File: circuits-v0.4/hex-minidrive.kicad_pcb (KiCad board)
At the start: 4 copper layers, 18 x 48 mm, 81 parts, among them X1 16MHz

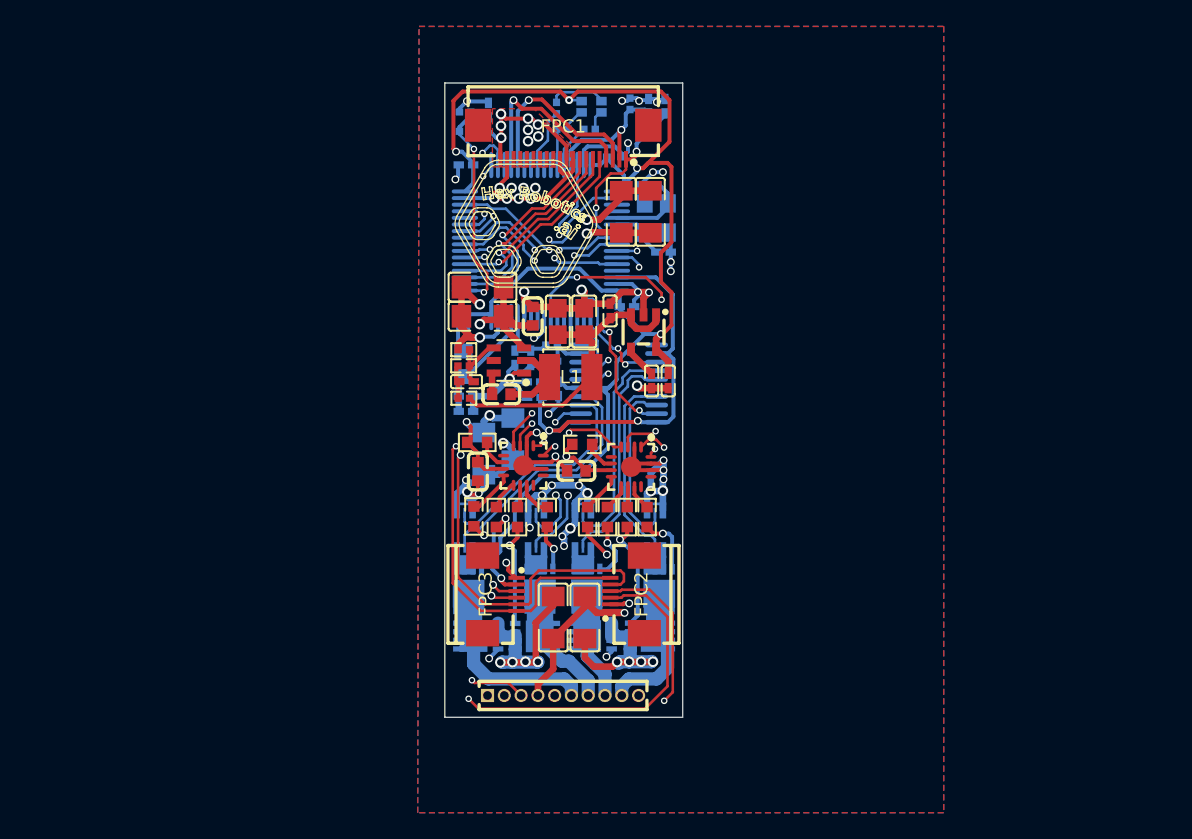
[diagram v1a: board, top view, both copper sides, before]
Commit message: Make schematic for v0.4 driver circuit.
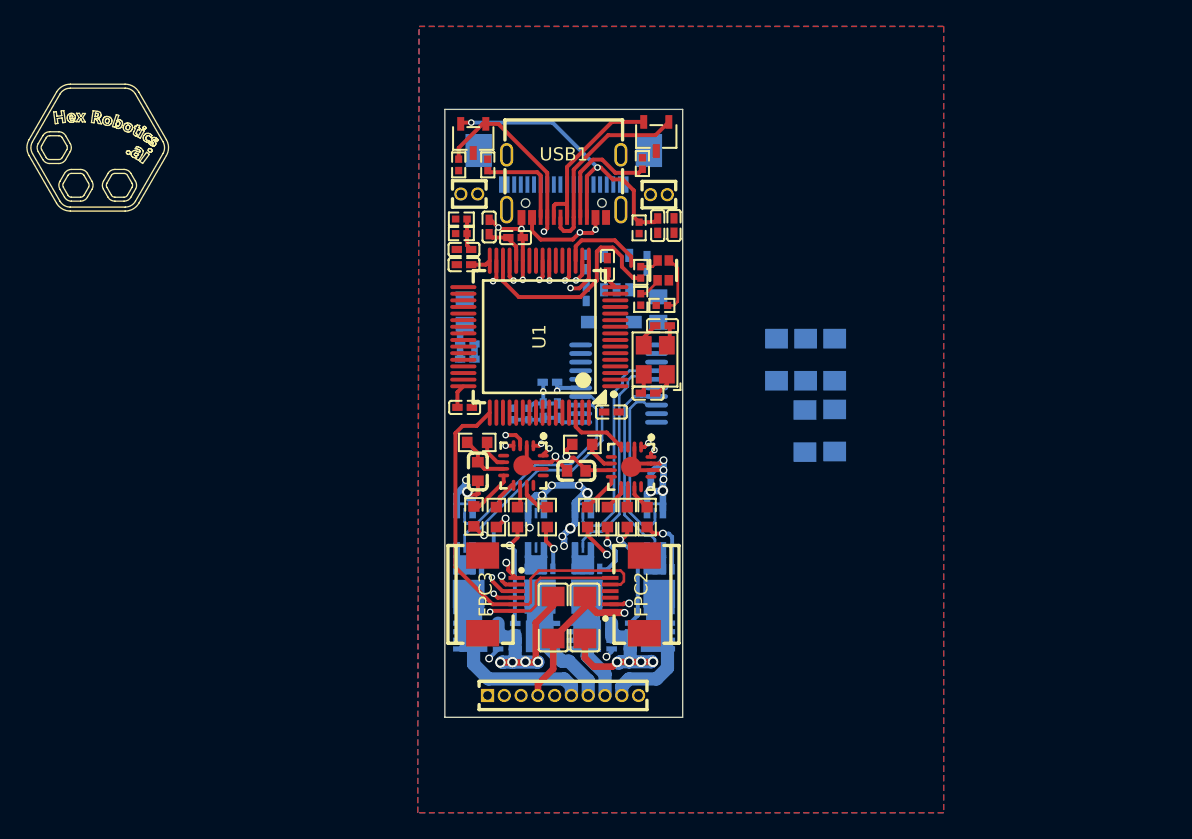
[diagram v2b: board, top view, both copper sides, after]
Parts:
- removed C41: 10uF, Library:C1206
- removed C42, C43: 100nF, Library:C0603
- removed C44, C45: 22uF, Library:C0805
- removed C46: 100pF, Library:C0402
- removed L1: 15uH, Library:IND-SMD_L4.0-W4.0
- removed R41: 49.9Ω, Library:R0402
- removed R42: 100kΩ, Library:R0402
- removed R43: 13.3kΩ, Library:R0402
- removed U4: ~, Library:SOT-23-6_L2.9-W1.6-P0.95-LS2.8-BL
- added D1: ~, Library:SOD-123_L2.7-W1.6-LS3.7-RD-1, B.Cu at (31.6, 38.1)
- added D2: ~, Library:SOT-23-3_L3.0-W1.7-P0.95-LS2.9-BR, F.Cu at (35.0, 24.1)
- added D3: ~, Library:SOT-23-3_L3.0-W1.7-P0.95-LS2.9-BR, F.Cu at (21.1, 24.2)
- added H2: 2P-1.27mm-header, Library:HDR-TH_2P-P1.27-V-M-2, F.Cu at (35.2, 28.4)
- added H3: 2P-1.27mm-header, Library:HDR-TH_2P-P1.27-V-M-2, F.Cu at (20.9, 28.4)
- added L3: 300mΩ, Library:L0805, B.Cu at (35.1, 37.1)
- added R14: 10kΩ, Library:R0402, F.Cu at (20.1, 26.2)
- added R5: 5.1kΩ, Library:R0402, F.Cu at (22.2, 26.2)
- added R6: 5.1kΩ, Library:R0402, F.Cu at (34.0, 26.1)
- added USB1: ~, Library:USB-C-SMD_TYPE-C16PIN, F.Cu at (28.0, 27.8)
- C103, C104, C105, C106, C109, C110, C111, C112, C113, C114, C115, LED1, R11, R15, R16, R17, R18, R19, U1, X1: moved to F.Cu
- C2, C3, C31, C32, C33, C5, FPC1, U3: moved to B.Cu
- moved C4 24.4 mm to (46.2, 46.3)
- moved C6 24.4 mm to (48.5, 46.3)
- moved C5 22.9 mm to (44.1, 40.9), turned to 90 degrees
- moved C111 19.3 mm to (31.6, 44.9)
- moved C2 17.9 mm to (48.5, 40.9), turned to 90 degrees
- moved C3 17.9 mm to (46.3, 40.9), turned to 90 degrees
- moved R16 16.9 mm to (35.4, 36.8), turned to 180 degrees
- moved C103 15.8 mm to (34.4, 43.5)
- moved C112 14.5 mm to (20.5, 44.5)
- moved R17 14.2 mm to (33.8, 36.4), turned to 90 degrees
- moved LED1 13.5 mm to (35.5, 34.2), turned to -90 degrees
- moved C109 13.1 mm to (31.3, 33.8), turned to -90 degrees
- moved R15 11.5 mm to (33.8, 34.3), turned to -90 degrees
- moved X1 10.7 mm to (34.9, 41.0), turned to 90 degrees
- moved C115 10.7 mm to (20.4, 32.6), turned to 0 degrees
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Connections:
- FPC1 pad 1: NRST -> VCC
- FPC1 pad 12: VCC -> GND
- FPC1 pad 14: VCC -> GND
- FPC1 pad 16: VCC -> GND
- FPC1 pad 18: VCC -> GND
- FPC1 pad 2: BOOT0/STOP -> VCC
- FPC1 pad 20: VCC -> GND
- FPC1 pad 3: USART3_RX -> VCC
- FPC1 pad 4: USART3_TX -> VCC
- FPC1 pad 5: SPI2_MOSI -> VCC
- FPC1 pad 6: SPI2_MISO -> VCC
- FPC1 pad 7: SPI2_SCK -> VCC
- FPC1 pad 8: SPI2_NSS -> VCC
- FPC1 pad 9: GND -> VCC
- R13 pad 2: VREF -> 3V3A
- R15 pad 2: TIM4_CH2/GREEN_LED -> TIM2_CH3/GREEN_LED
- R17 pad 1: TIM4_CH1/RED_LED -> TIM2_CH1/RED_LED
- U1 pad 13: unconnected-(U1-PA1-Pad13) -> TIM2_CH2/BLUE_LED
- U1 pad 19: unconnected-(U1-PA5-Pad19) -> TIM2_CH1/RED_LED
- U1 pad 30: unconnected-(U1-PB10-Pad30) -> TIM2_CH3/GREEN_LED
- U1 pad 34: SPI2_NSS -> unconnected-(U1-PB12-Pad34)
- U1 pad 35: SPI2_SCK -> unconnected-(U1-PB13-Pad35)
- U1 pad 36: SPI2_MISO -> TIM1_CH2N
- U1 pad 37: SPI2_MOSI -> unconnected-(U1-PB15-Pad37)
- U1 pad 45: unconnected-(U1-PA11-Pad45) -> USB_D_N
- U1 pad 46: TIM1_CH2N -> USB_D_P
- U1 pad 52: USART3_TX -> unconnected-(U1-PC10-Pad52)
- U1 pad 53: USART3_RX -> unconnected-(U1-PC11-Pad53)
- U1 pad 56: TIM2_CH2/BLUE_LED -> unconnected-(U1-PB3-Pad56)
- U1 pad 59: TIM4_CH1/RED_LED -> unconnected-(U1-PB6-Pad59)
- U1 pad 60: TIM4_CH2/GREEN_LED -> unconnected-(U1-PB7-Pad60)
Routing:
- net 3V3: track 144.5 -> 27.0 mm, vias 6 -> 3
- net GND: track 165.3 -> 78.0 mm, vias 49 -> 23
- net I2C2_SCL: track 69.6 -> 0.00 mm, vias 2 -> 0
- net I2C2_SDA: track 68.1 -> 0.00 mm, vias 2 -> 0
- net SYS_JTCK-SWCLK: track 51.2 -> 11.2 mm, vias 2 -> 1
- net TIM3_CH2/ENCODER_2: track 39.0 -> 0.00 mm, vias 1 -> 0
- net TIM3_CH1/ENCODER_1: track 37.5 -> 0.00 mm, vias 1 -> 0
- net I2C3_SCL: track 36.6 -> 1.86 mm, vias 2 -> 1
- net VCC: track 73.8 -> 39.3 mm, vias 21 -> 9
- net I2C3_SDA: track 36.3 -> 2.45 mm, vias 2 -> 1
- net TIM3_CH3/ENCODER_3: track 34.1 -> 1.55 mm, vias 2 -> 1
- net ADC1_IN3/HALF_VREF: track 37.2 -> 5.23 mm, vias 2 -> 0
- net TIM1_CH4N: track 25.3 -> 1.51 mm, vias 3 -> 1
- net 5V: track 23.4 -> 0.00 mm
- net TIM1_CH1N: track 23.9 -> 0.60 mm, vias 2 -> 1
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- removed copper zone on F.Cu, net VCC
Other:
- board size 18 x 48 mm -> 18 x 46 mm

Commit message: Almost done re-wiring v0.4
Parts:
- moved C2 24.2 mm to (72.7, 41.0)
- moved C3 24.2 mm to (70.5, 41.0)
- moved C4 24.2 mm to (70.4, 46.4)
- moved C6 24.2 mm to (72.7, 46.3)
- moved C5 24.2 mm to (68.2, 41.0)
- moved L3 10.1 mm to (28.4, 29.7), turned to 0 degrees
- moved C107 7.20 mm to (20.5, 43.2), turned to 0 degrees
- moved C108 6.55 mm to (20.5, 42.0), turned to 0 degrees
- moved R13 6.52 mm to (20.4, 39.8), turned to 180 degrees
- moved R12 6.39 mm to (20.4, 41.0), turned to 0 degrees
- moved C21 5.63 mm to (25.6, 48.1)
- moved C33 5.62 mm to (34.2, 30.2), turned to 180 degrees
- moved D1 5.49 mm to (30.9, 32.6), turned to 90 degrees
- moved C109 4.48 mm to (35.0, 36.2), turned to 0 degrees
- moved U2 4.45 mm to (31.0, 47.0)
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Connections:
- R15 pad 2: TIM2_CH3/GREEN_LED -> TIM2_CH1/GREEN_LED
- R17 pad 1: TIM2_CH1/RED_LED -> TIM2_CH3/RED_LED
- U1 pad 19: TIM2_CH1/RED_LED -> TIM2_CH1/GREEN_LED
- U1 pad 30: TIM2_CH3/GREEN_LED -> TIM2_CH3/RED_LED
- U2 pad 2: ADC1_IN1/M1_CURRENT -> ADC2_IN3/M2_CURRENT
- U2 pad 3: -Probe-1 -> -Probe-2
- U2 pad 4: +Probe-1 -> +Probe-2
- U2 pad 6: +Probe-2 -> +Probe-1
- U2 pad 7: -Probe-2 -> -Probe-1
- U2 pad 8: ADC2_IN3/M2_CURRENT -> ADC1_IN1/M1_CURRENT
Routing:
- net 3V3: track 27.0 -> 123.6 mm, vias 3 -> 7
- net I2C2_SCL: track 0.00 -> 52.5 mm, vias 0 -> 2
- net I2C2_SDA: track 0.00 -> 51.5 mm, vias 0 -> 2
- net ADC1_IN3/HALF_VREF: track 5.23 -> 48.6 mm, vias 0 -> 5
- net TIM3_CH3/ENCODER_3: track 1.55 -> 42.9 mm
- net TIM3_CH2/ENCODER_2: track 0.00 -> 34.1 mm, vias 0 -> 1
- net TIM3_CH1/ENCODER_1: track 0.00 -> 32.6 mm, vias 0 -> 1
- net NRST: track 14.4 -> 44.7 mm, vias 1 -> 4
- net I2C3_SCL: track 1.86 -> 27.5 mm, vias 1 -> 2
- net I2C3_SDA: track 2.45 -> 25.6 mm, vias 1 -> 2
- net BOOT0/STOP: track 23.5 -> 45.1 mm, vias 2 -> 4
- net SYS_JTCK-SWCLK: track 11.2 -> 32.4 mm, vias 1 -> 0
- net ADC2_IN17/M4_CURRENT: track 1.71 -> 22.0 mm
- net TIM1_CH4N: track 1.51 -> 20.3 mm, vias 1 -> 2
- net GND: track 78.0 -> 96.6 mm, vias 23 -> 27
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
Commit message: Tentatively done wiring v0.4.
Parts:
- removed C5, C6: 10uF, Library:C1206
- moved C4 51.9 mm to (20.4, 32.2)
- moved C3 50.6 mm to (20.5, 48.8)
- moved C2 49.1 mm to (24.2, 32.6), turned to 180 degrees
- moved C107 2.06 mm to (22.4, 44.0), turned to 90 degrees
- moved C108 1.81 mm to (20.6, 43.9)
- moved R12 1.81 mm to (20.6, 42.8)
- moved R13 1.81 mm to (20.6, 41.5)
- moved C101 1.81 mm to (20.6, 39.2)
- moved C102 1.81 mm to (20.6, 40.4)
- moved L2 1.81 mm to (20.4, 36.8)
- moved C103 1.10 mm to (35.5, 43.6)
- moved R102 0.50 mm to (21.1, 52.3)
- moved R202 0.25 mm to (24.8, 52.9)
- moved C110 0.10 mm to (32.4, 31.7)
- moved C104 0.06 mm to (35.5, 38.4)
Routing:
- net GND: track 96.6 -> 121.1 mm, vias 27 -> 37
- net VCC: track 50.4 -> 59.1 mm, vias 10 -> 12
- net TIM1_CH2: track 14.2 -> 16.2 mm
- net 3V3: track 123.6 -> 121.7 mm
- net ADC1_IN3/HALF_VREF: track 48.6 -> 46.9 mm
- net BOOT0/STOP: track 45.1 -> 44.0 mm
- net TIM2_CH3/RED_LED: track 11.2 -> 11.9 mm
- net TIM3_CH2/ENCODER_2: track 34.1 -> 34.8 mm

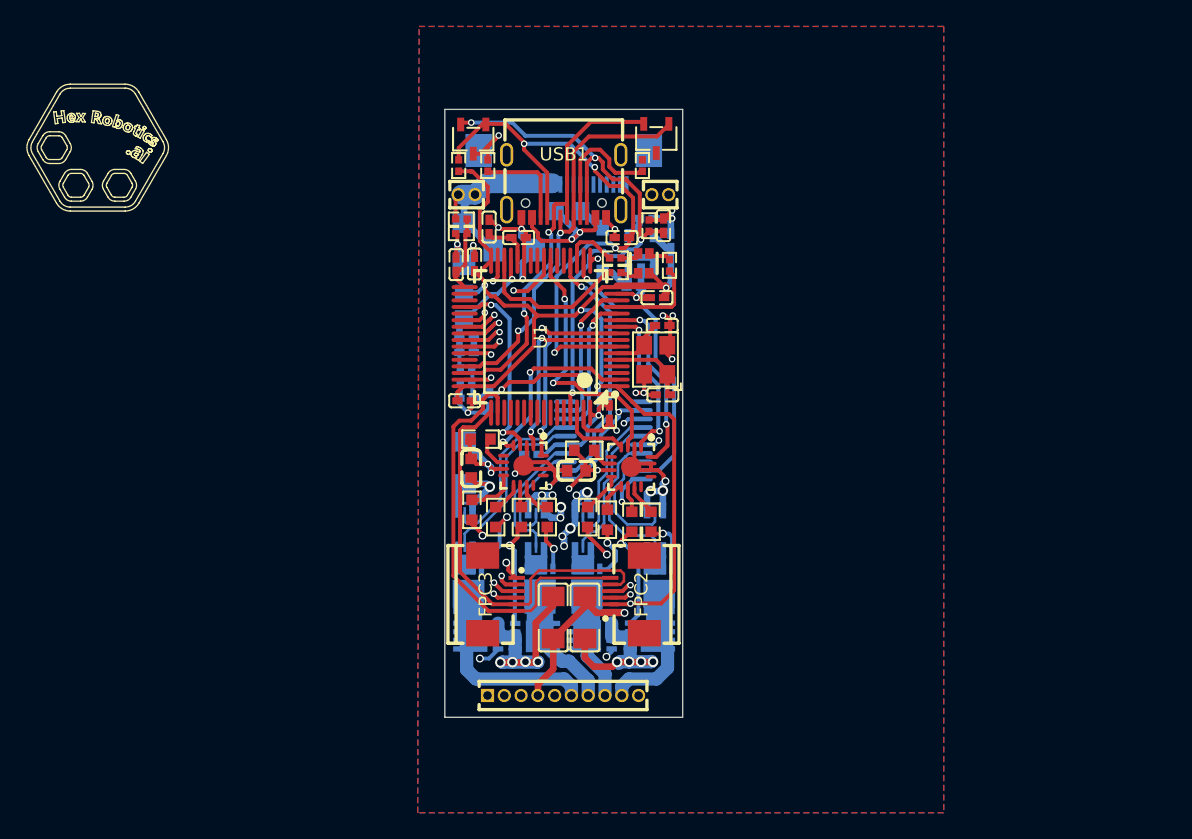
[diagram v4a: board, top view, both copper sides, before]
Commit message: Finish and generate production files for v0.4 driver circuit.
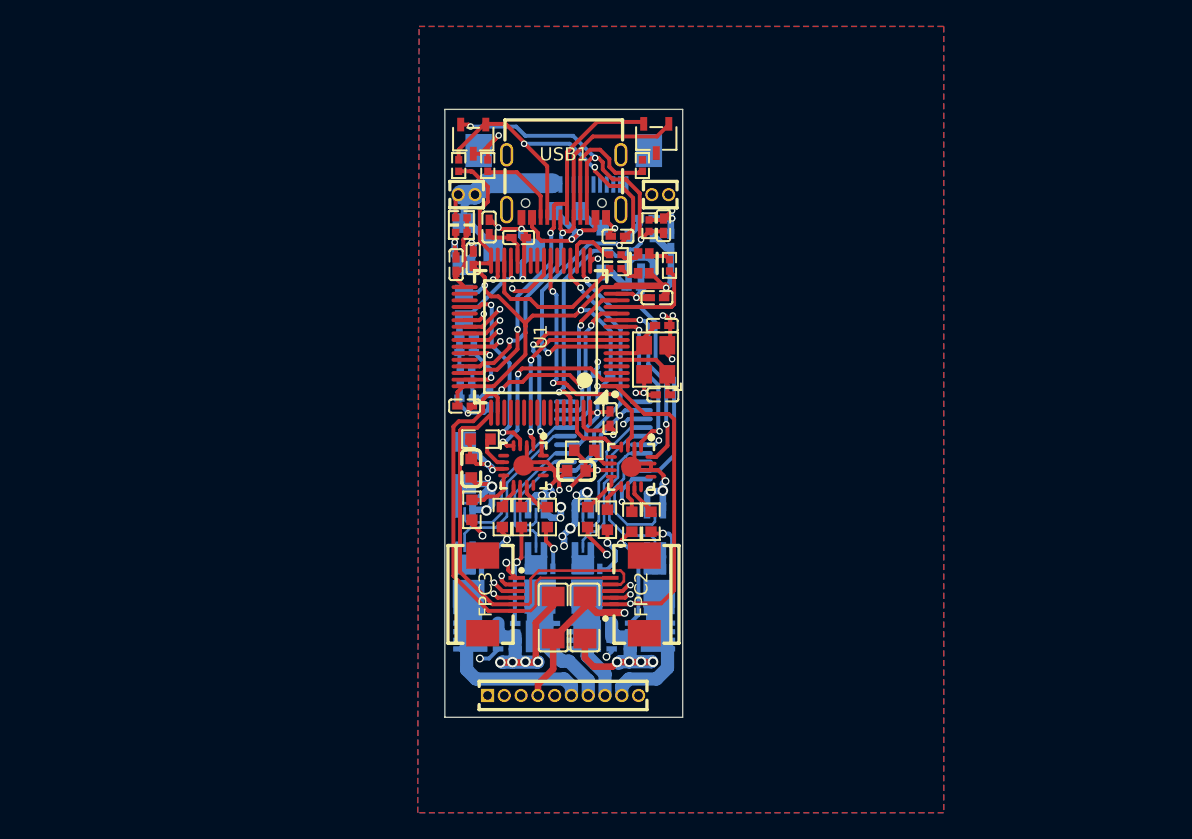
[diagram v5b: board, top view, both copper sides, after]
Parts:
- moved C21 8.12 mm to (31.0, 42.1)
- moved R101 0.50 mm to (23.4, 52.9)
- moved C111 0.45 mm to (31.5, 45.4)
- moved C113 0.41 mm to (21.1, 33.3)
- moved C112 0.40 mm to (20.5, 44.5)
- moved C110 0.32 mm to (32.1, 31.6)
- moved R17 0.30 mm to (31.9, 34.0)
- moved R15 0.25 mm to (31.9, 33.0)
- moved R18 0.10 mm to (20.2, 30.2)
- moved L3 0.10 mm to (28.3, 29.7)
- moved R19 0.10 mm to (20.2, 31.3)
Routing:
- net GND: track 121.1 -> 129.5 mm, vias 37 -> 40
- net 3V3: track 121.7 -> 119.6 mm
- net /Gate-1-Negative: track 5.90 -> 4.19 mm
- net TIM3_CH2/ENCODER_2: track 34.8 -> 36.0 mm
- net /USB:CC2: track 7.29 -> 6.39 mm
- net BOOT0/STOP: track 44.0 -> 44.9 mm
- net ADC1_IN3/HALF_VREF: track 46.9 -> 46.0 mm
- net TIM1_CH2: track 16.2 -> 15.4 mm
- net USB_D_P: track 31.3 -> 30.5 mm
- net -Probe-1: track 13.3 -> 12.7 mm
- net TIM1_CH1: track 14.3 -> 13.7 mm
- net TIM1_CH4N: track 19.8 -> 19.2 mm
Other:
- board text added: "8+2 VCC"
- board text added: "GND 2+8"
- board text added: "Kelvin contact resistor pattern"
- board text removed: "VCC GND ... SPI3_NSS SPI3_CLK SPI3_MISO SPI3_MOSI TX RX BOOT0 RESET"
